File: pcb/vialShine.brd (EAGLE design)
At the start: 7 x 7 mm, 5 parts

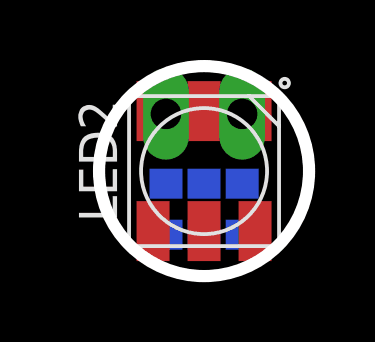
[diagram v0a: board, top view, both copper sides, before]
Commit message: Added simple 5050 LED and resistors.
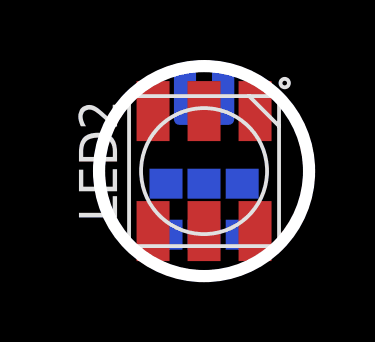
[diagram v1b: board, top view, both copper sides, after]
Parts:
- removed JP1: (no value), pinhead:1X02
- added J1: PINHEAD_SMD_2X1, vialShine:PINHEAD_SMD_2X1
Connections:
- net N$2: now also J1.2; no longer JP1.2
- net N$3: now also J1.1; no longer JP1.1
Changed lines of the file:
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@@
 </autorouter>
 <elements>
-<element name="JP1" library="pinhead" package="1X02" value="" x="0" y="1.905" rot="MR0"/>
 <element name="R1" library="rcl" package="R0603" value="" x="0" y="-1.27" rot="MR270"/>
 <element name="R2" library="rcl" package="R0603" value="" x="-1.27" y="-1.27" rot="MR270"/>
 <element name="R3" library="rcl" package="R0603" value="" x="1.27" y="-1.27" rot="MR270"/>
 <element name="LED2" library="adafruit" package="RGBLED5050" value="RGBLED5050" x="0" y="0" rot="R90"/>
+<element name="J1" library="vialShine" package="PINHEAD_SMD_2X1" value="PINHEAD_SMD_2X1" x="0" y="2.54" rot="MR0"/>
 </elements>
 <signals>
@@
 <contactref element="R1" pad="1"/>
 <contactref element="R2" pad="1"/>
-<contactref element="JP1" pad="2"/>
-<wire x1="0" y1="-0.42" x2="1.27" y2="-0.42" width="0" layer="19" extent="16-16"/>
+<contactref element="J1" pad="2"/>
+<wire x1="0" y1="-0.42" x2="-0.635" y2="2.54" width="0" layer="19" extent="16-16"/>
+<wire x1="1.27" y1="-0.42" x2="0" y2="-0.42" width="0" layer="19" extent="16-16"/>
 <wire x1="-1.27" y1="-0.42" x2="0" y2="-0.42" width="0" layer="19" extent="16-16"/>
-<wire x1="-1.27" y1="1.905" x2="-1.27" y2="-0.42" width="0" layer="19" extent="16-16"/>
 </signal>
 <signal name="N$4">
@@
 <contactref element="LED2" pad="6"/>
 <contactref element="LED2" pad="4"/>
-<contactref element="JP1" pad="1"/>
 <contactref element="LED2" pad="5"/>
-<wire x1="0" y1="2" x2="-1.7" y2="2" width="0" layer="19" extent="1-1"/>
-<wire x1="1.27" y1="1.905" x2="0" y2="2" width="0" layer="19" extent="1-1"/>
-<wire x1="1.7" y1="2" x2="1.27" y2="1.905" width="0" layer="19" extent="1-1"/>
+<contactref element="J1" pad="1"/>
+<wire x1="0" y1="2" x2="0.635" y2="2.54" width="0" layer="19" extent="1-16"/>
+<wire x1="1.7" y1="2" x2="0.635" y2="2.54" width="0" layer="19" extent="1-16"/>
+<wire x1="-1.7" y1="2" x2="0" y2="2" width="0" layer="19" extent="1-1"/>
 </signal>
 </signals>
